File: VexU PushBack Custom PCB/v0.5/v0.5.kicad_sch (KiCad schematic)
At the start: 39 parts, among them J1 4P4C, J2 Conn_01x04_Pin, U1 Teensy4.1, U2 MP2338GTL-P, U3 4069, U4 MAX485E

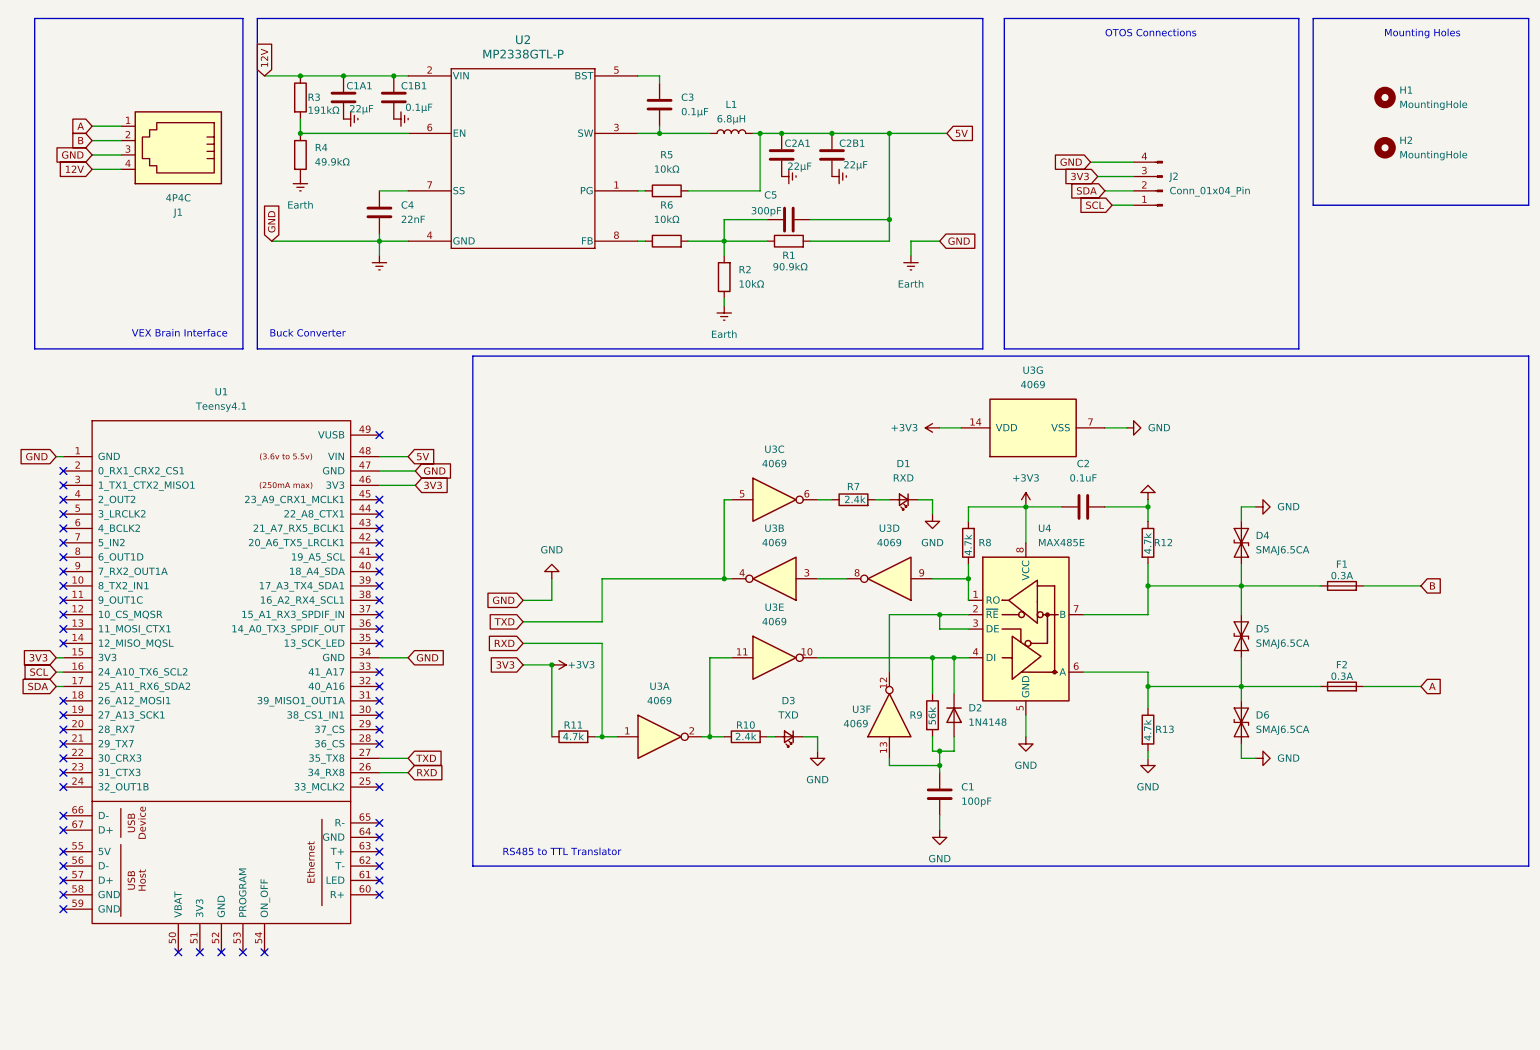
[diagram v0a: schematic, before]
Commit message: Schematic fully done
will need to keep working on tracing and component layout
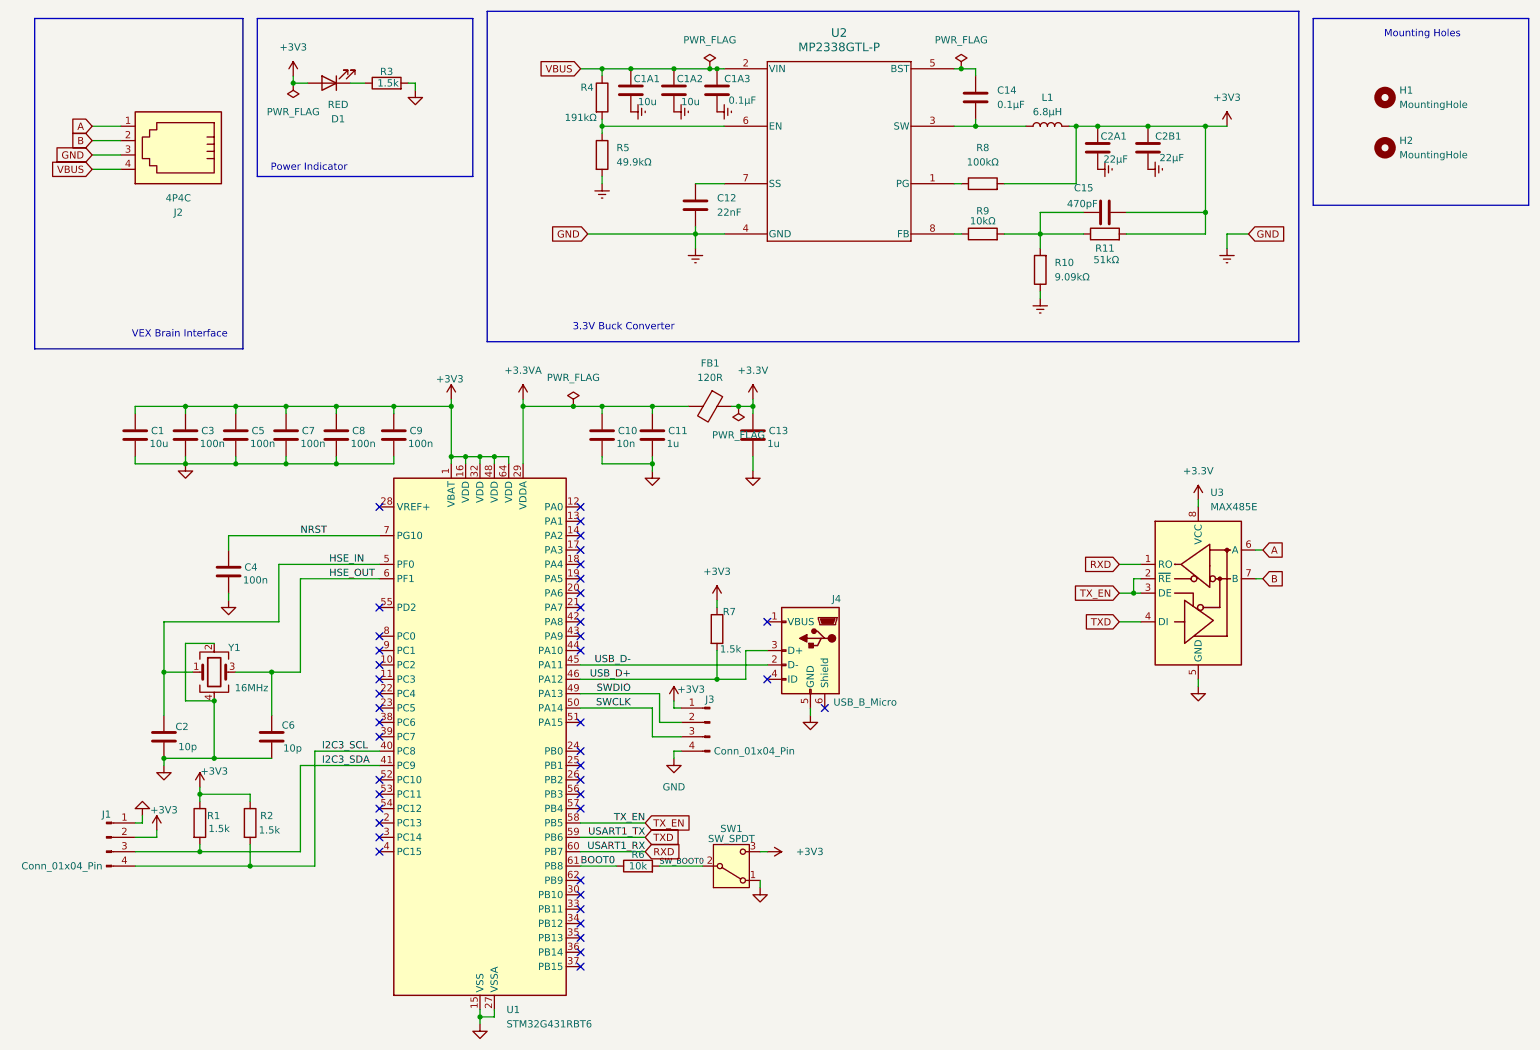
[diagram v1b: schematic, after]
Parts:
- removed D1: RXD, LED_SMD:LED_0402_1005Metric, symbol Device:LED_Small
- removed D2: 1N4148, Diode_THT:D_DO-35_SOD27_P7.62mm_Horizontal, symbol Diode:1N4148
- removed D3: TXD, LED_SMD:LED_0402_1005Metric, symbol Device:LED_Small
- removed D4, D5, D6: SMAJ6.5CA, Diode_SMD:D_SMA, symbol Diode:SMAJ6.5CA
- removed F1, F2: 0.3A, Fuse:Fuse_0603_1608Metric, symbol Device:Fuse
- removed J2: Conn_01x04_Pin, Connector_PinHeader_1.27mm:PinHeader_1x04_P1.27mm_Horizontal, symbol Connector:Conn_01x04_Pin
- removed R10: 2.4k, Resistor_SMD:R_0402_1005Metric, symbol Device:R
- removed R11, R12, R13, R8: 4.7k, Resistor_SMD:R_0402_1005Metric, symbol Device:R
- removed R9: 56k, Resistor_SMD:R_0402_1005Metric, symbol Device:R
- removed U1: Teensy4.1, teensy.pretty-master:Teensy41, symbol teensy:Teensy4.1
- removed U3: 4069, Package_DIP:DIP-14_W7.62mm, symbol 4xxx:4069
- removed U4: MAX485E, Package_SO:SOIC-8_3.9x4.9mm_P1.27mm, symbol Interface_UART:MAX485E
- added C10: 10n, Capacitor_SMD:C_0402_1005Metric, symbol Device:C
- added C11, C13: 1u, Capacitor_SMD:C_0402_1005Metric, symbol Device:C
- added C1A1: 10u, Capacitor_SMD:C_1206_3216Metric, symbol Device:C
- added C3, C4, C5, C7, C8, C9: 100n, Capacitor_SMD:C_0402_1005Metric, symbol Device:C
- added C6: 10p, Capacitor_SMD:C_0402_1005Metric, symbol Device:C
- added D1: RED, LED_SMD:LED_0603_1608Metric, symbol Device:LED
- added FB1: 120R, Inductor_SMD:L_0603_1608Metric, symbol Device:FerriteBead
- added J1: Conn_01x04_Pin, Connector_PinHeader_2.54mm:PinHeader_1x04_P2.54mm_Horizontal, symbol Connector:Conn_01x04_Pin
- added J3: Conn_01x04_Pin, Connector_PinHeader_2.54mm:PinHeader_1x04_P2.54mm_Vertical, symbol Connector:Conn_01x04_Pin
- added J4: USB_B_Micro, Connector_USB:USB_Micro-B_Molex_47346-0001, symbol Connector:USB_B_Micro
- added R1, R2, R3: 1.5k, Resistor_SMD:R_0402_1005Metric, symbol Device:R
- added R6: 10k, Resistor_SMD:R_0402_1005Metric, symbol Device:R
- added SW1: SW_SPDT, Button_Switch_SMD:SW_SPST_B3S-1100, symbol Switch:SW_SPDT
- added U1: STM32G431RBT6, Package_QFP:LQFP-64_10x10mm_P0.5mm, symbol MCU_ST_STM32G4:STM32G431RBTx
- added U3: MAX485E, Package_SO:SOIC-8_3.9x4.9mm_P1.27mm, symbol Interface_UART:MAX485E
- added Y1: 16MHz, Crystal:Crystal_SMD_3225-4Pin_3.2x2.5mm, symbol Device:Crystal_GND24
- C1: value 100pF -> 10u
- C15: renamed from C5; value 300pF -> 470pF
- C1A2: renamed from C1A1; value 22μF -> 10u
- C2: value 0.1uF -> 10p
- R10: renamed from R2; value 10kΩ -> 9.09kΩ
- R11: renamed from R1; value 90.9kΩ -> 51kΩ
- R7: value 2.4k -> 1.5k
- R8: renamed from R5; value 10kΩ -> 100kΩ
- renumbered C4 to C12, C3 to C14, C1B1 to C1A3, J1 to J2, R3 to R4, R4 to R5, R6 to R9
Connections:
- net 5V is gone; now on net +3V3: C15.2, C2A1.1, C2B1.1, L1.2, R11.2, R8.2
- net +3V3: now also C1.1, R7.1, C3.1, C5.1, C7.1, C8.1, C9.1, D1.2 (A), J1.2 (Pin_2), J3.1 (Pin_1), R1.1, R2.1, SW1.3 (C), U1.1 (VBAT), U1.16 (VDD), U1.32 (VDD), U1.48 (VDD), U1.64 (VDD); no longer C2.1
- net A: now also U3.6 (A)
- net B: now also U3.7 (B)
- net Earth: now also C10.2, C11.2, C13.2, C1A1.2, C3.2, C4.2, C5.2, C6.2, C7.2, C8.2, C9.2, J1.1 (Pin_1), J3.4 (Pin_4), J4.5 (GND), R3.2, SW1.1 (A), U1.15 (VSS), U1.27 (VSSA), U1.31 (VSS), U1.47 (VSS), U1.63 (VSS), U3.5 (GND), Y1.2, Y1.4
- net RXD: now also U1.60 (PB7), U3.1 (RO)
- net TXD: now also U1.59 (PB6), U3.4 (DI)
- net USB_D+: now reaches R7.2
- net USB_D+: now also J4.3 (D+), U1.46 (PA12)
- net 12V renamed VBUS
- net VBUS: now also C1A1.1
- new net: D1.1 (K), R3.1
- new net +3.3V: C13.1, FB1.1, U3.8 (VCC)
- new net +3.3VA: C10.1, C11.1, FB1.2, U1.29 (VDDA)
- new net BOOT0: R6.1, U1.61 (PB8)
- new net HSE_IN: C2.1, U1.5 (PF0), Y1.1
- new net HSE_OUT: C6.1, U1.6 (PF1), Y1.3
- new net I2C3_SCL: J1.4 (Pin_4), R2.2, U1.40 (PC8)
- new net I2C3_SDA: J1.3 (Pin_3), R1.2, U1.41 (PC9)
- new net NRST: C4.1, U1.7 (PG10)
- new net SWCLK: J3.3 (Pin_3), U1.50 (PA14)
- new net SWDIO: J3.2 (Pin_2), U1.49 (PA13)
- new net SW_BOOT0: R6.2, SW1.2 (B)
- new net TX_EN: U1.58 (PB5), U3.2 (~{RE}), U3.3 (DE)
- new net USB_D-: J4.2 (D-), U1.45 (PA11)
- no-connect marks 57 -> 43
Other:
- note added: "3.3V Buck Converter"
- note added: "Power Indicator"
- note removed: "Buck Converter"
- note removed: "OTOS Connections"
- note removed: "RS485 to TTL Translator"
- moved on the sheet: C12, C14, C15, C1A2, C1A3, C2A1, C2B1, L1, R10, R11, R4, R5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

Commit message: Layout of buck convertr
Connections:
- net +3V3: now also R3.1; no longer D1.2 (A)
- net Earth: now also D1.1 (K); no longer R3.2
- new net: D1.2 (A), R3.2
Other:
- moved on the sheet: D1, R3
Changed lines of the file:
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@@
 	(symbol
 		(lib_id "Device:R")
-		(at 80.01 26.67 90)
+		(at 69.85 26.67 90)
 		(unit 1)
 		(exclude_from_sim no)
@@
 		(dnp no)
 		(property "Reference" "R3"
-			(at 80.01 24.638 90)
+			(at 69.85 24.638 90)
 			(effects
 				(font
@@
 		)
 		(property "Value" "1.5k"
-			(at 80.264 26.67 90)
+			(at 69.85 26.67 90)
 			(effects
 				(font
@@
 		)
 		(property "Footprint" "Resistor_SMD:R_0402_1005Metric"
-			(at 80.01 28.448 90)
-			(effects
-				(font
-					(size 1.27 1.27)
-				)
-				(hide yes)
-			)
-		)
-		(property "Datasheet" "~"
-			(at 80.01 26.67 0)
+			(at 69.85 28.448 90)
+			(effects
+				(font
+					(size 1.27 1.27)
+				)
+				(hide yes)
+			)
+		)
+		(property "Datasheet" "~"
+			(at 69.85 26.67 0)
 			(effects
 				(font
@@
 		)
 		(property "Description" "Resistor"
-			(at 80.01 26.67 0)
+			(at 69.85 26.67 0)
 			(effects
 				(font
@@
 	(symbol
 		(lib_id "Device:LED")
-		(at 69.85 26.67 180)
+		(at 80.01 26.67 180)
 		(unit 1)
 		(exclude_from_sim no)
@@
 		(dnp no)
 		(property "Reference" "D1"
-			(at 71.4375 33.02 0)
+			(at 81.5975 33.02 0)
 			(effects
 				(font
@@
 		)
 		(property "Value" "RED"
-			(at 71.4375 30.48 0)
+			(at 81.5975 30.48 0)
 			(effects
 				(font
@@
 		)
 		(property "Footprint" "LED_SMD:LED_0603_1608Metric"
-			(at 69.85 26.67 0)
-			(effects
-				(font
-					(size 1.27 1.27)
-				)
-				(hide yes)
-			)
-		)
-		(property "Datasheet" "~"
-			(at 69.85 26.67 0)
+			(at 80.01 26.67 0)
+			(effects
+				(font
+					(size 1.27 1.27)
+				)
+				(hide yes)
+			)
+		)
+		(property "Datasheet" "~"
+			(at 80.01 26.67 0)
 			(effects
 				(font
@@
 		)
 		(property "Description" "Light emitting diode"
-			(at 69.85 26.67 0)
+			(at 80.01 26.67 0)
 			(effects
 				(font
@@
 		)
 		(property "Sim.Pins" "1=K 2=A"
-			(at 69.85 26.67 0)
-			(effects
-				(font
+			(at 80.01 26.67 0)
+			(effects
+				(font

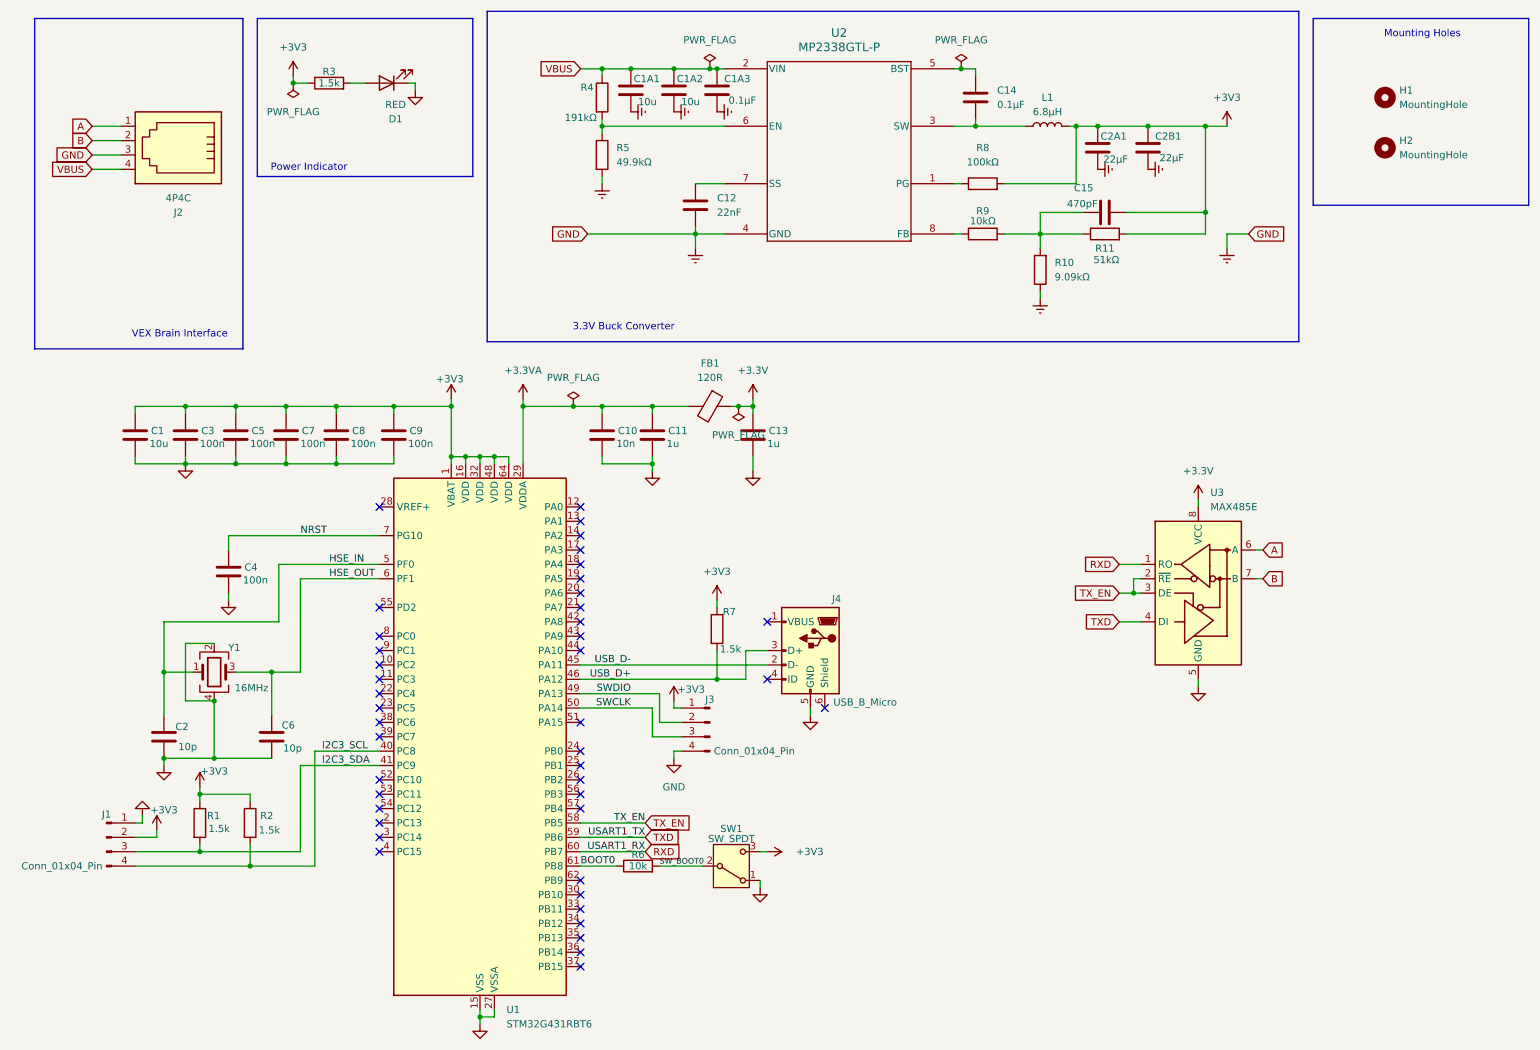
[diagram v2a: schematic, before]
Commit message: Different Partial Layout Design
Still have to do tracing and finishing layout
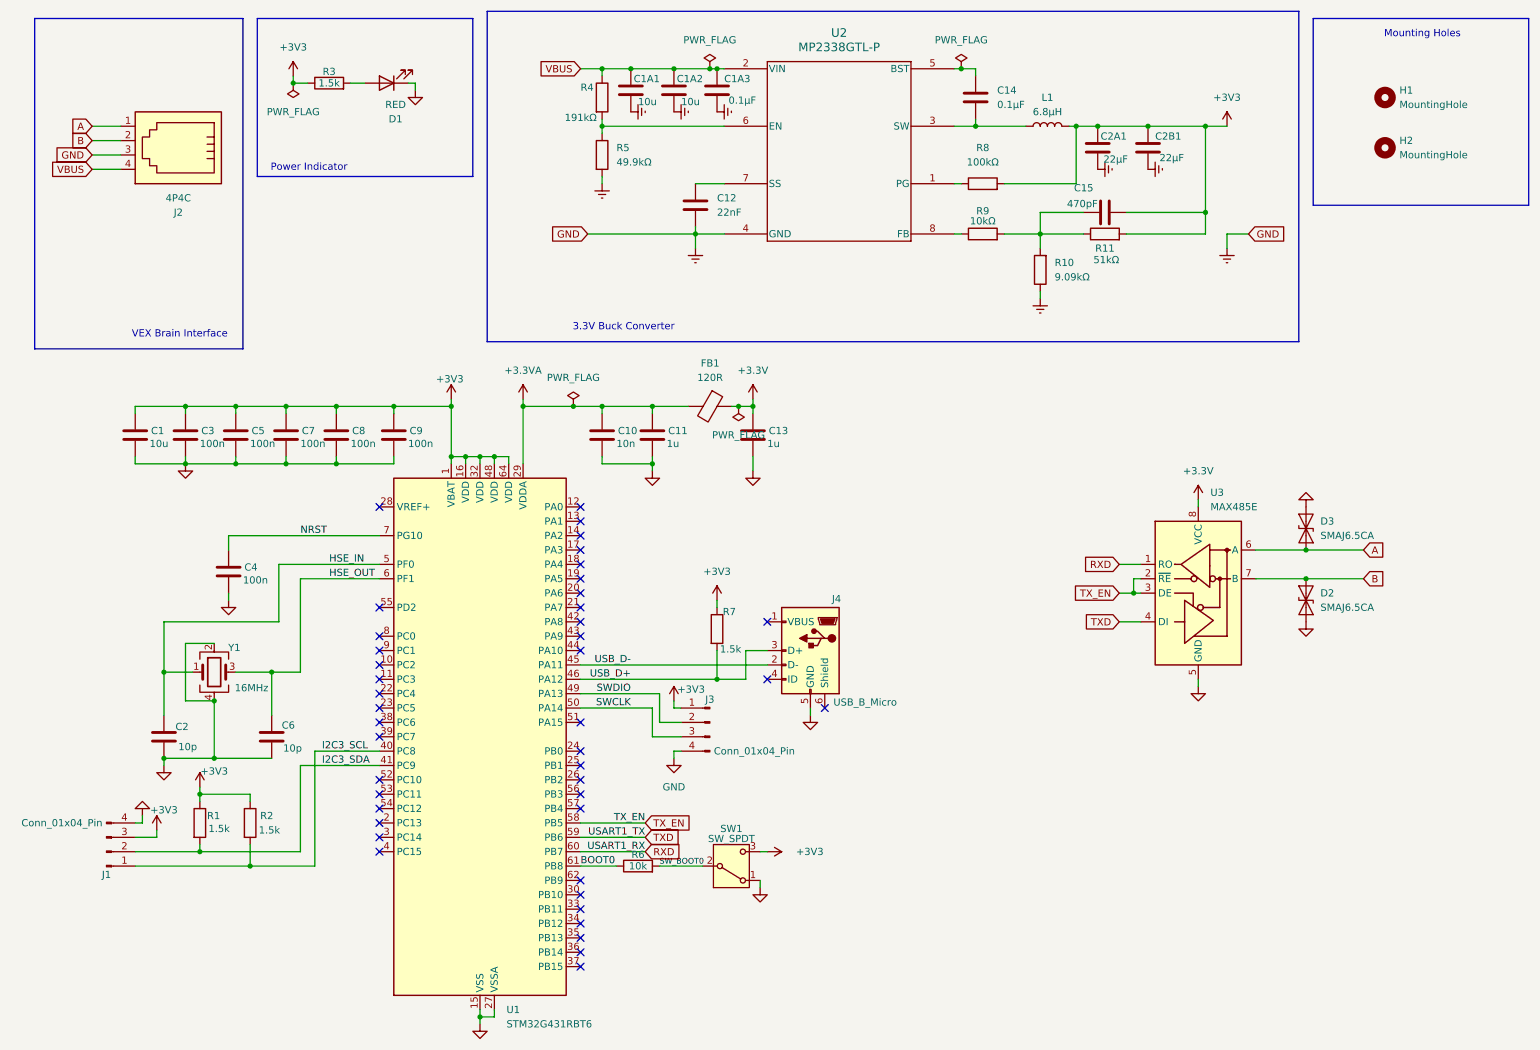
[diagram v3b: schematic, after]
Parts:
- added D2, D3: SMAJ6.5CA, Diode_SMD:D_SMA, symbol Diode:SMAJ6.5CA
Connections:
- net +3V3: now also J1.3 (Pin_3); no longer J1.2 (Pin_2)
- net A: now also D3.1 (A1)
- net B: now also D2.2 (A2)
- net Earth: now also J1.4 (Pin_4), D2.1 (A1), D3.2 (A2); no longer J1.1 (Pin_1)
- net I2C3_SCL: now also J1.1 (Pin_1); no longer J1.4 (Pin_4)
- net I2C3_SDA: now also J1.2 (Pin_2); no longer J1.3 (Pin_3)

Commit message: Layout redesign for tigher component placing
Changed switch sized and mad layout smaler
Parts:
- SW1: footprint Button_Switch_SMD:SW_SPST_B3S-1100 -> Button_Switch_SMD:SW_SPST_B3U-1100P
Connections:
- net A: now also D3.2 (A2); no longer D3.1 (A1)
- net Earth: now also D3.1 (A1); no longer D3.2 (A2)
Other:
- moved on the sheet: D3
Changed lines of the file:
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@@
 	)
 	(junction
+		(at 242.57 109.22)
+		(diameter 0)
+		(color 0 0 0 0)
+	)
+	(junction
 		(at 181.61 24.13)
 		(diameter 0)
@@
 	)
 	(junction
-		(at 242.57 109.22)
-		(diameter 0)
-		(color 0 0 0 0)
-	)
-	(junction
 		(at 144.78 83.82)
 		(diameter 0)
@@
 	(wire
 		(pts
+			(xy 242.57 109.22) (xy 252.73 109.22)
+		)
+		(stroke
+			(width 0)
+			(type default)
+		)
+	)
+	(wire
+		(pts
 			(xy 212.09 114.3) (xy 212.09 116.84)
 		)
@@
 	(wire
 		(pts
-			(xy 242.57 109.22) (xy 252.73 109.22)
-		)
-		(stroke
-			(width 0)
-			(type default)
-		)
-	)
-	(wire
-		(pts
 			(xy 55.88 152.4) (xy 46.99 152.4)
 		)
@@
 			)
 		)
-		(property "Footprint" "Button_Switch_SMD:SW_SPST_B3S-1100"
+		(property "Footprint" "Button_Switch_SMD:SW_SPST_B3U-1100P"
 			(at 140.97 165.1 0)
 			(effects
@@
 	(symbol
 		(lib_id "Diode:SMAJ6.5CA")
-		(at 242.57 105.41 90)
+		(at 242.57 105.41 270)
 		(unit 1)
 		(exclude_from_sim no)
@@
 					(size 1.27 1.27)
 				)
-				(justify right)
+				(justify left)
 			)
 		)
@@
 					(size 1.27 1.27)
 				)
-				(justify right)
+				(justify left)
 			)
 		)
 		(property "Footprint" "Diode_SMD:D_SMA"
-			(at 247.65 105.41 0)
+			(at 237.49 105.41 0)
 			(effects
 				(font
